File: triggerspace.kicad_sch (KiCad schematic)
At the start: 128 parts, among them J1 Conn_01x2, J10 Conn_01x12, J11 Conn_01x12, J12 Conn_02x05_Odd_Even, J13 Conn_01x10, J14 Conn_01x10, J15 Conn_01x10, J2 Conn_01x2, J3 Conn_01x4, J4 Conn_01x4, J5 Conn_01x3, J6 Conn_01x3, J7 Conn_01x10, J8 Conn_01x3, Q1 2N3904, Q2 2N3904, U1 MCP6002_1, U2 MCP6002_1, U3 MCP6002_1, U4 L7805, U5 LM4040LP-5, U6 74HC595, U8 6N138, X1 CV_X, Y1 CV_Y

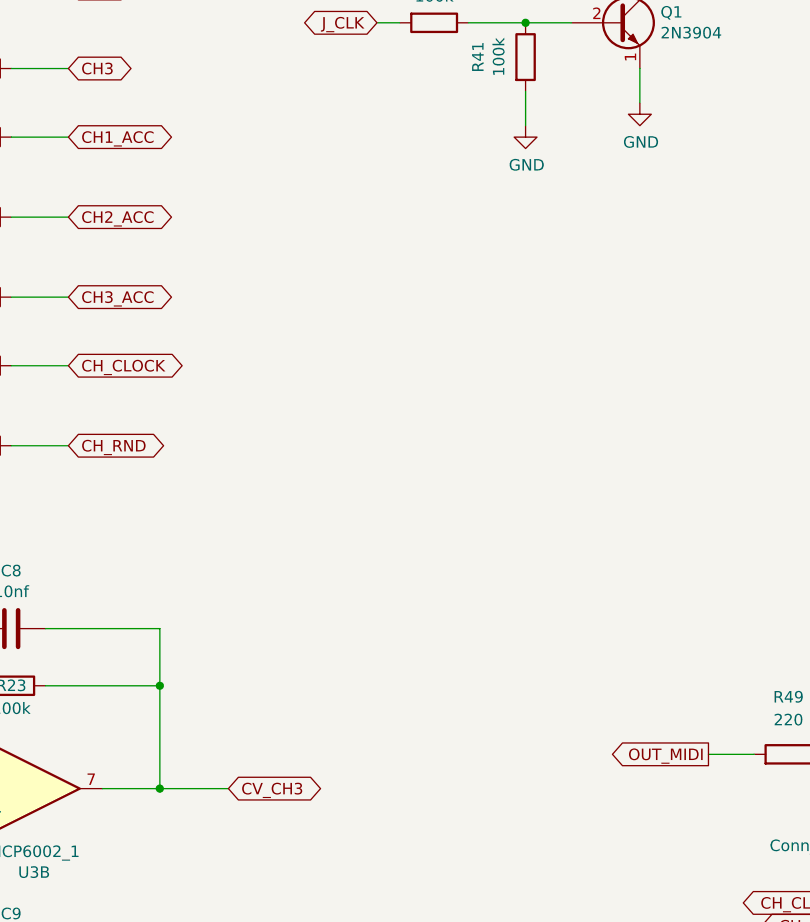
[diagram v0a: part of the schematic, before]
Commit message: Hardware: socketed RC reconstruction caps on the six output jacks
Adds J16..J21 (2.54mm 1x02 sockets) on the jack PCB's back copper, one per
audio output jack. Pin 1 taps the channel net on the jack side of the 1k
series resistor (R32..R37 on the back board); pin 2 lands in the GND pour.
Plugging a capacitor in forms a first-order reconstruction low-pass with the
existing 1k; pulling it out disables the filter, so the cap value stays a
run-time choice rather than a layout commitment.

J16 CH1, J17 CH2, J18 CH3, J19 CH1_ACC, J20 CH2_ACC, J21 CH3_ACC.

The 1k resistors are unchanged - they already set the expected ~1k Eurorack
output impedance and double as the filter's series R.

Placement was clearance-solved against existing pads, tracks and courtyards;
each socket routes to its jack tip pad with a single 2.24mm B.Cu track, and
GND needs no routing (full GND zones on both layers). Socket outlines moved
to B.Fab as the back silkscreen is congested there.

Note: pcbnew 9 re-serialised the .kicad_pcb (KiCad 8 -> 9 format) and
refilled the zones, which cleared pre-existing stale-fill DRC violations.
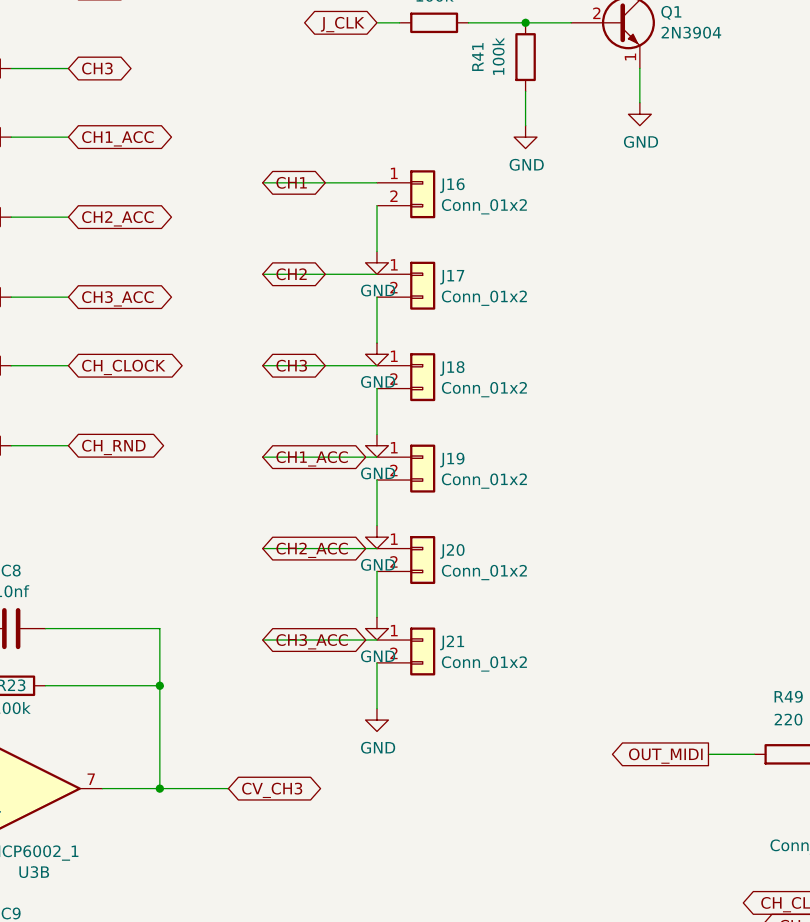
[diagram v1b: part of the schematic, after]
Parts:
- added J16, J17, J18, J19, J20, J21: Conn_01x2, Connector_PinSocket_2.54mm:PinSocket_1x02_P2.54mm_Vertical, symbol Connector_Generic:Conn_01x02
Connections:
- net CH1: now also J16.1 (Pin_1)
- net CH1_ACC: now also J19.1 (Pin_1)
- net CH2: now also J17.1 (Pin_1)
- net CH2_ACC: now also J20.1 (Pin_1)
- net CH3: now also J18.1 (Pin_1)
- net CH3_ACC: now also J21.1 (Pin_1)
- net GND: now also J16.2 (Pin_2), J17.2 (Pin_2), J18.2 (Pin_2), J19.2 (Pin_2), J20.2 (Pin_2), J21.2 (Pin_2)

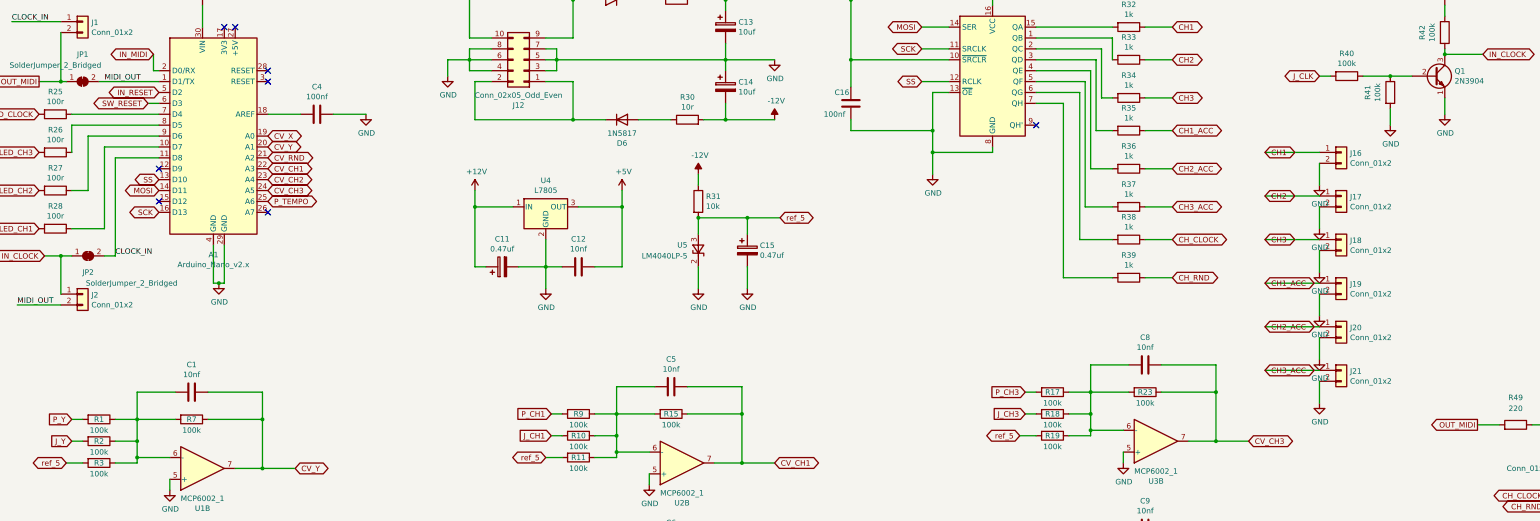
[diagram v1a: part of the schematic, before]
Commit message: Fixed cap socket placement by hand
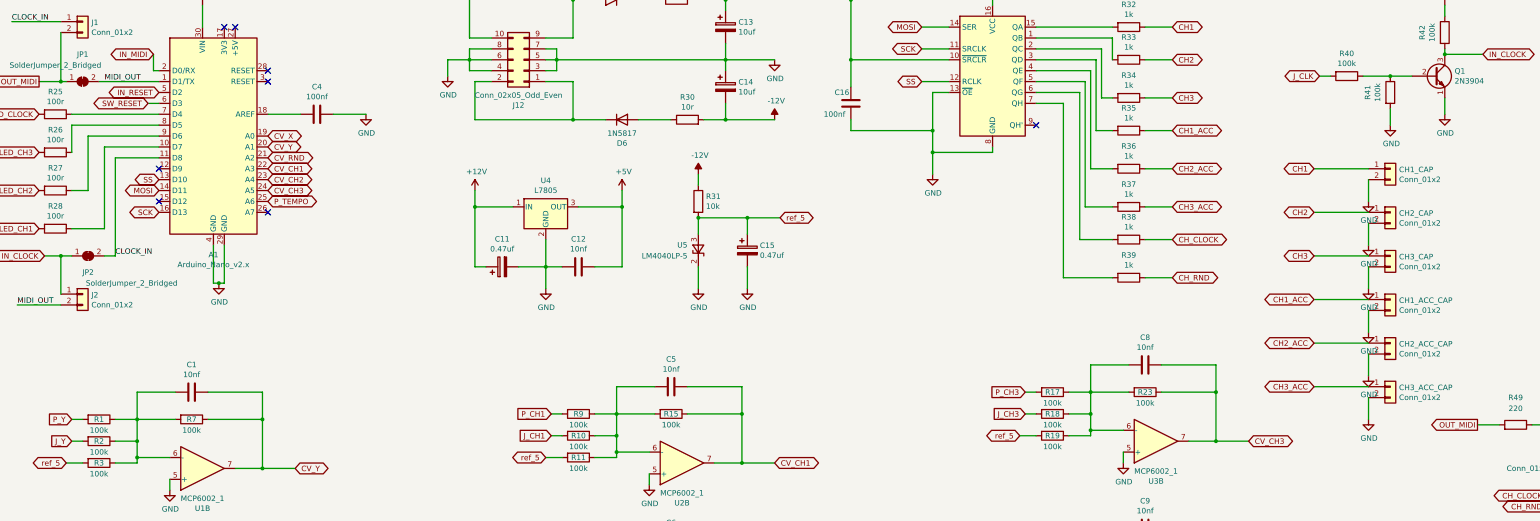
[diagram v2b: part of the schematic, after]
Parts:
- renumbered J19 to CH1_ACC_CAP, J16 to CH1_CAP, J20 to CH2_ACC_CAP, J17 to CH2_CAP, J21 to CH3_ACC_CAP, J18 to CH3_CAP
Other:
- moved on the sheet: CH1_ACC_CAP, CH1_CAP, CH2_ACC_CAP, CH2_CAP, CH3_ACC_CAP, CH3_CAP

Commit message: Bump version to v0.5.0, regenerate back_pcb/jack_pcb fab outputs
Version bump (schematic title-block rev, PCB silkscreen text on both boards)
reflects the RC reconstruction-cap sockets added on the jack PCB's six audio
outputs. README documents the new revision as pending bench verification,
keeping the v0.042 notes as historical build/bodge record.

Regenerated gerbers, drill, position files, netlist, and BOM for back_pcb and
jack_pcb to pick up the cap-socket placement fix and the new silkscreen text.
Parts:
- renumbered CH1_ACC_CAP to CH1_ACC_CAP1, CH1_CAP to CH1_CAP1, CH2_ACC_CAP to CH2_ACC_CAP1, CH2_CAP to CH2_CAP1, CH3_ACC_CAP to CH3_ACC_CAP1, CH3_CAP to CH3_CAP1
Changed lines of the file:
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@@
 		(title "triggerspace (\"NanoGris-MIDI\")")
 		(date "2020-03-28")
-		(rev "0.042")
+		(rev "0.5.0")
 		(company "Andrew Perry (semi-sensible synth)")
 	)
@@
 		(on_board yes)
 		(dnp no)
-		(property "Reference" "CH1_ACC_CAP"
+		(property "Reference" "CH1_ACC_CAP1"
 			(at 353.822 96.7232 0)
 			(effects
@@
 			(project "triggerspace"
 				(path "/a5cd8da1-8f7f-4f80-bb23-0317de562222"
-					(reference "CH1_ACC_CAP")
+					(reference "CH1_ACC_CAP1")
 					(unit 1)
 				)
@@
 		(on_board yes)
 		(dnp no)
-		(property "Reference" "CH1_CAP"
+		(property "Reference" "CH1_CAP1"
 			(at 353.822 66.2432 0)
 			(effects
@@
 			(project "triggerspace"
 				(path "/a5cd8da1-8f7f-4f80-bb23-0317de562222"
-					(reference "CH1_CAP")
+					(reference "CH1_CAP1")
 					(unit 1)
 				)
@@
 		(on_board yes)
 		(dnp no)
-		(property "Reference" "CH3_ACC_CAP"
+		(property "Reference" "CH3_ACC_CAP1"
 			(at 353.822 117.0432 0)
 			(effects
@@
 			(project "triggerspace"
 				(path "/a5cd8da1-8f7f-4f80-bb23-0317de562222"
-					(reference "CH3_ACC_CAP")
+					(reference "CH3_ACC_CAP1")
 					(unit 1)
 				)
@@
 		(on_board yes)
 		(dnp no)
-		(property "Reference" "CH2_CAP"
+		(property "Reference" "CH2_CAP1"
 			(at 353.822 76.4032 0)
 			(effects
@@
 			(project "triggerspace"
 				(path "/a5cd8da1-8f7f-4f80-bb23-0317de562222"
-					(reference "CH2_CAP")
+					(reference "CH2_CAP1")
 					(unit 1)
 				)
@@
 		(on_board yes)
 		(dnp no)
-		(property "Reference" "CH2_ACC_CAP"
+		(property "Reference" "CH2_ACC_CAP1"
 			(at 353.822 106.8832 0)
 			(effects
@@
 			(project "triggerspace"
 				(path "/a5cd8da1-8f7f-4f80-bb23-0317de562222"
-					(reference "CH2_ACC_CAP")
+					(reference "CH2_ACC_CAP1")
 					(unit 1)
 				)
@@
 		(on_board yes)
 		(dnp no)
-		(property "Reference" "CH3_CAP"
+		(property "Reference" "CH3_CAP1"
 			(at 353.822 86.5632 0)
 			(effects
@@
 			(project "triggerspace"
 				(path "/a5cd8da1-8f7f-4f80-bb23-0317de562222"
-					(reference "CH3_CAP")
+					(reference "CH3_CAP1")
 					(unit 1)
 				)

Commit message: Nano VIN from +12V, LED resistors, MIDI header labels/refdes, fix fab outputs
- A1 VIN (pin 30) moved from +5V to +12V, removing the v0.042 bodge. The +5V
  rail junction moves off pad 30 to a new via; VIN is routed on B.Cu to U4 IN.
- R25-R28 (LED resistors) 100r -> 4.7k, with "RL" silkscreen labels.
- Back-board 2-pin MIDI socket: was a PCB-only footprint duplicating the jack
  board's J4. Renamed J9 and added to the schematic on IN_MIDI/OUT_MIDI.
  Front D0/RX and D1/TX labels were swapped; corrected, and MIDI IN/OUT
  labels added on the back silkscreen.
- Regenerated back_pcb/jack_pcb fab outputs. The previous v0.5.0 outputs
  included the other board's tracks, vias and zones in each zip; the board
  split now removes those too. The back BOM no longer lists the jack's J4.
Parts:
- added J9: Conn_01x2, Connector_PinSocket_2.54mm:PinSocket_1x02_P2.54mm_Vertical, symbol Connector_Generic:Conn_01x02
- R25, R26, R27, R28: value 100r -> 4.7k
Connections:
- net +12V: now also A1.30 (VIN)
- net +5V: no longer A1.30 (VIN)
- net IN_MIDI: now also J9.1 (Pin_1)
- net OUT_MIDI: now also J9.2 (Pin_2)
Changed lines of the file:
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@@
 	)
 	(symbol
-		(lib_id "NanoGris-rescue:+5V-power-GridsNanoV3-rescue")
+		(lib_id "NanoGris-rescue:+12V-power-GridsNanoV3-rescue")
 		(at 74.93 27.94 0)
 		(unit 1)
@@
 			)
 		)
-		(property "Value" "+5V"
+		(property "Value" "+12V"
 			(at 75.311 23.5458 0)
 			(effects
@@
 			)
 		)
-		(property "Value" "100r"
+		(property "Value" "4.7k"
 			(at 40.64 50.3936 90)
 			(effects
@@
 			)
 		)
-		(property "Value" "100r"
+		(property "Value" "4.7k"
 			(at 40.64 77.0636 90)
 			(effects
@@
 			)
 		)
-		(property "Value" "100r"
+		(property "Value" "4.7k"
 			(at 40.64 68.1736 90)
 			(effects
@@
 			)
 		)
-		(property "Value" "100r"
+		(property "Value" "4.7k"
 			(at 40.64 59.2836 90)
 			(effects
@@
 			)
 		)
+	)
+	(symbol
+		(lib_id "Connector_Generic:Conn_01x02")
+		(at 35.56 20.32 0)
+		(unit 1)
+		(exclude_from_sim no)
+		(in_bom yes)
+		(on_board yes)
+		(dnp no)
+		(property "Reference" "J9"
+			(at 37.592 20.5232 0)
+			(effects
+				(font
+					(size 1.27 1.27)
+				)
+				(justify left)
+			)
+		)
+		(property "Value" "Conn_01x2"
+			(at 37.592 22.8346 0)
+			(effects
+				(font
+					(size 1.27 1.27)
+				)
+				(justify left)
+			)
+		)
+		(property "Footprint" "Connector_PinSocket_2.54mm:PinSocket_1x02_P2.54mm_Vertical"
+			(at 35.56 20.32 0)
+			(effects
+				(font
+					(size 1.27 1.27)
+				)
+				(hide yes)
+			)
+		)
+		(property "Datasheet" "~"
+			(at 35.56 20.32 0)
+			(effects
+				(font
+					(size 1.27 1.27)
+				)
+				(hide yes)
+			)
+		)
+		(property "Description" ""
+			(at 35.56 20.32 0)
+			(effects
+				(font
+					(size 1.27 1.27)
+				)
+				(hide yes)
+			)
+		)
+		(pin "1"
+		)
+		(pin "2"
+		)
+		(instances
+			(project "triggerspace"
+				(path "/a5cd8da1-8f7f-4f80-bb23-0317de562222"
+					(reference "J9")
+					(unit 1)
+				)
+			)
+		)
+	)
+	(wire
+		(pts
+			(xy 25.4 20.32) (xy 30.48 20.32)
+		)
+		(stroke
+			(width 0)
+			(type default)
+		)
+	)
+	(wire
+		(pts
+			(xy 25.4 22.86) (xy 30.48 22.86)
+		)
+		(stroke
+			(width 0)
+			(type default)
+		)
+	)
+	(global_label "IN_MIDI"
+		(shape bidirectional)
+		(at 25.4 20.32 180)
+		(fields_autoplaced yes)
+		(effects
+			(font
+				(size 1.27 1.27)
+			)
+			(justify right)
+		)
+		(property "Intersheetrefs" "${INTERSHEET_REFS}"
+			(at 15.2826 20.32 0)
+			(effects
+				(font
+					(size 1.27 1.27)
+				)
+				(justify right)
+				(hide yes)
+			)
+		)
+	)
+	(global_label "OUT_MIDI"
+		(shape bidirectional)
+		(at 25.4 22.86 180)
+		(fields_autoplaced yes)
+		(effects
+			(font
+				(size 1.27 1.27)
+			)
+			(justify right)
+		)
+		(property "Intersheetrefs" "${INTERSHEET_REFS}"
+			(at 15.2826 22.86 0)
+			(effects
+				(font
+					(size 1.27 1.27)
+				)
+				(justify right)
+				(hide yes)
+			)
+		)

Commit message: U4 lies flat (TO-220 tab-down), back PCB outline shifted 1mm
- U4 (L7805) swapped to TO-220-3_Horizontal_TabDown, pin 1 at (165.0, 78.5),
  body lying over the free area above J7. Only the GND pour is on F.Cu under
  the tab (with GND stitching vias); +5V/+12V rerouted on B.Cu or between the
  pin row and the body. C12 moved up 0.94mm to make room.
- Back PCB outline (and its zones) moved 1mm (-x in the file, right as seen
  from the front panel). Parts and inter-board headers are unchanged; checked
  against all 33 mating header/standoff pins that the left edge is now flush
  with the jack PCB to within 0.09mm.
- Regenerated back_pcb/jack_pcb fab outputs.
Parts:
- U4: footprint Package_TO_SOT_THT:TO-220-3_Vertical -> Package_TO_SOT_THT:TO-220-3_Horizontal_TabDown
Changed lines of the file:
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@@
 			)
 		)
-		(property "Footprint" "Package_TO_SOT_THT:TO-220-3_Vertical"
+		(property "Footprint" "Package_TO_SOT_THT:TO-220-3_Horizontal_TabDown"
 			(at 155.575 78.74 0)
 			(effects
